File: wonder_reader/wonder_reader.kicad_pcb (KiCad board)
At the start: 2 copper layers, 168 x 77 mm, 114 parts, among them J1 USB_C_Receptacle_USB2.0, J2 ffc_solenoid, J3 speaker_socket, J4 batt_conn, J5 motor_connection, J8 vibrator, J9 TF-115, SW10 SW_keb, SW11 SW_keb, SW12 SW_keb, SW13 SW_keb, SW14 SW_keb, SW15 SW_keb, SW16 SW_keb, SW17 SW_keb, SW2 SW_keb, SW3 SW_keb, SW4 SW_keb, SW5 motor_limit, SW6 SW_keb, SW7 SW_keb, SW8 SW_keb, SW9 onoffswitch, U1 ESP32-S3-WROOM-1, U10 MAX98357AETE+T, U12 STM32L031G6Ux, U2 DRV8837C, U4 BQ25895RTWR, U5 TLV62569DBV, U6 DRV8837C, U7 DRV8837C, U8 DRV8837C, U9 DRV8837C

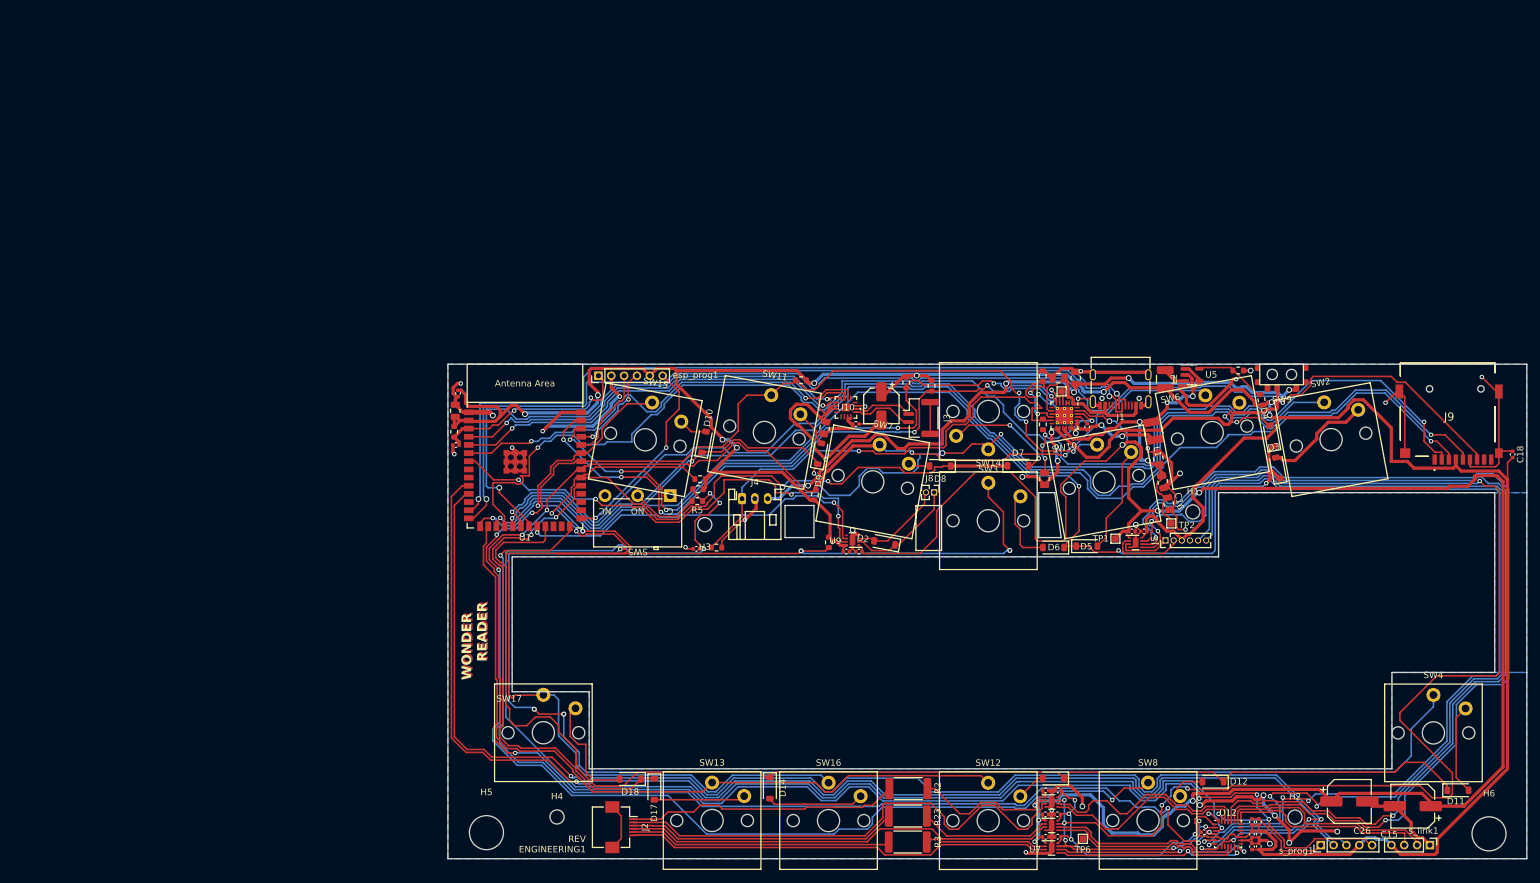
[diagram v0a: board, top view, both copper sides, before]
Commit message: Updated pcb to lower costs and rectify faults
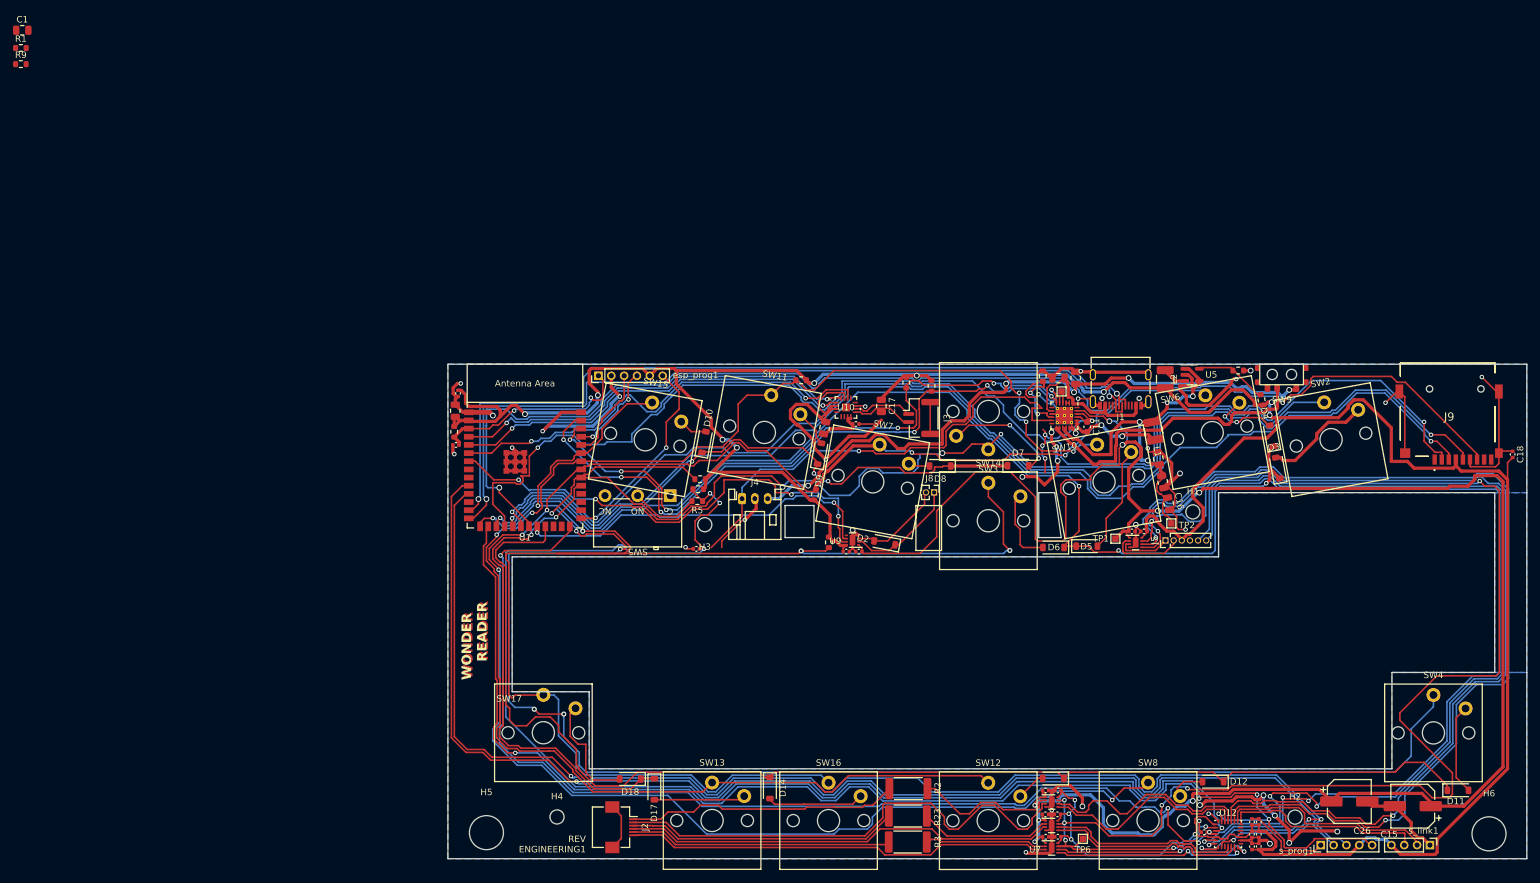
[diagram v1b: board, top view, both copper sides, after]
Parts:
- removed C12: 10uf, Capacitor_SMD:C_0805_2012Metric
- removed R14: 5.23k, Resistor_SMD:R_0603_1608Metric
- removed R15: 30.1k, Resistor_SMD:R_0603_1608Metric
- added C1: 4.7uf, Capacitor_SMD:C_0805_2012Metric, F.Cu at (1.73, 1.00)
- added R1: 10k, Resistor_SMD:R_0603_1608Metric, F.Cu at (1.50, 3.77)
- added R9: 10k, Resistor_SMD:R_0603_1608Metric, F.Cu at (1.50, 6.28)
- C11: footprint Capacitor_SMD:C_0402_1005Metric -> Capacitor_SMD:C_0603_1608Metric
- C17: value 33uf -> 10uf; footprint Capacitor_SMD:CP_Elec_5x5.4 -> Capacitor_SMD:C_0805_2012Metric
- R16: value 442k -> 270k
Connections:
- J4 pad 1: /t_pin -> unconnected-(J4-Pin_1-Pad1)
- U4 pad 11: /t_pin -> Net-(U4-TS)
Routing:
- net /t_pin: track 74.8 -> 0.00 mm, vias 1 -> 0
- net (no net): track 0.00 -> 74.8 mm, vias 0 -> 1
- net +BATT: track 51.6 -> 55.6 mm
- net Net-(SW9-B): track 45.0 -> 47.9 mm
- net +5V: track 311.0 -> 312.9 mm
